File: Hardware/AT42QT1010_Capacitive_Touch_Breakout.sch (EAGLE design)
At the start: 31 parts, among them Q1 600mA/40V, U1 AT42QT1010 - UDFN

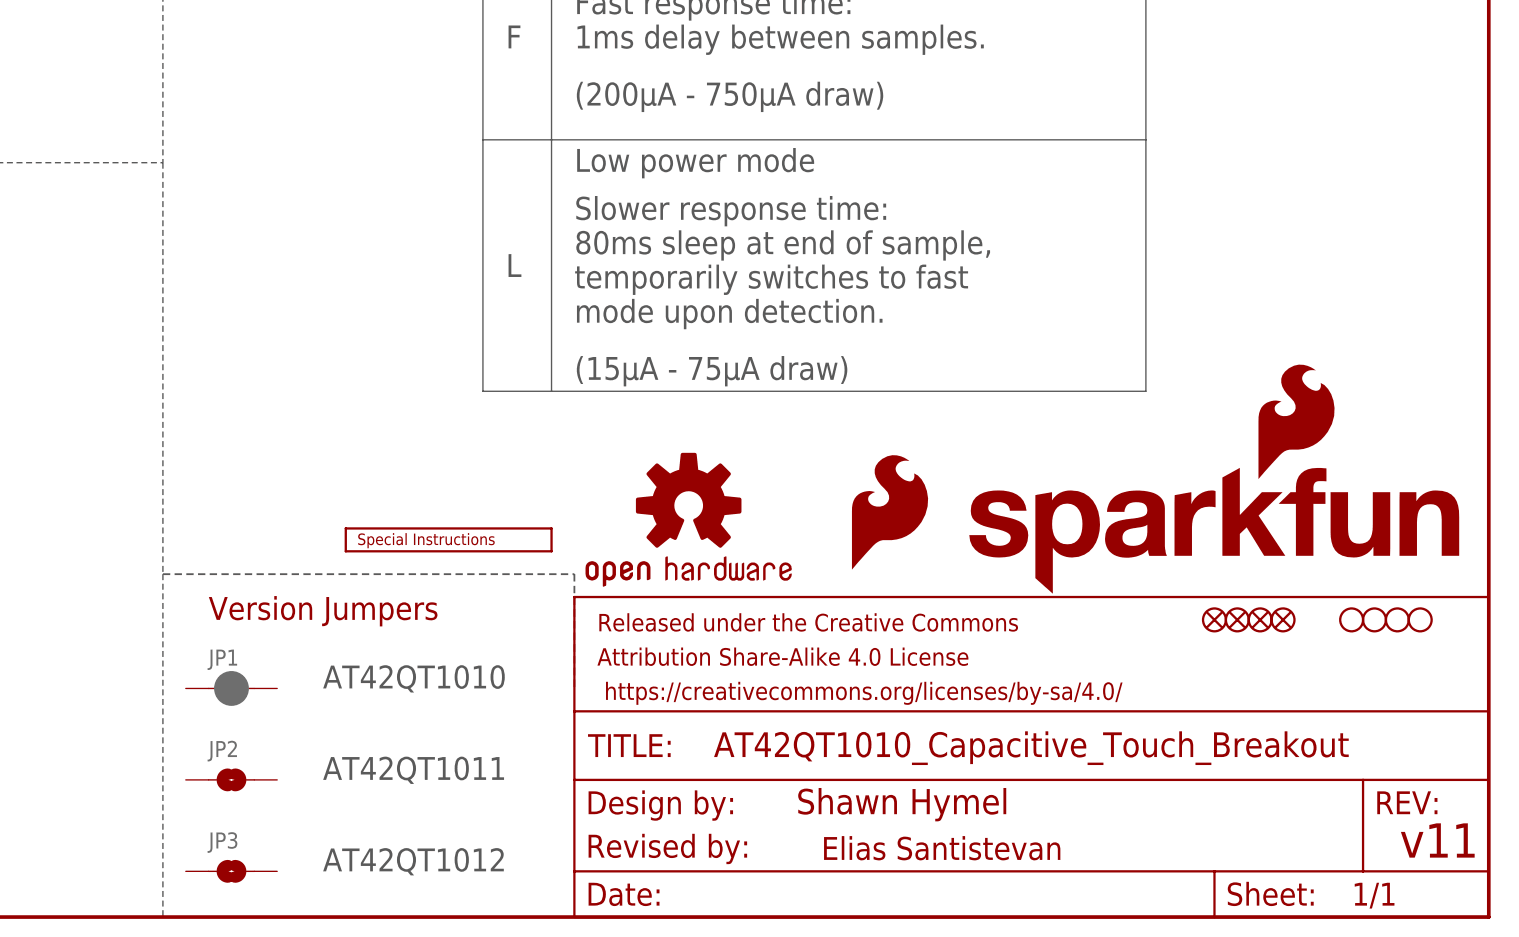
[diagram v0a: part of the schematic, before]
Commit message: Revert "Made space for and added version jumpers"
This reverts commit 0dfcf3fd33d472c1ea0c54a853371dbd5ffd3b83.
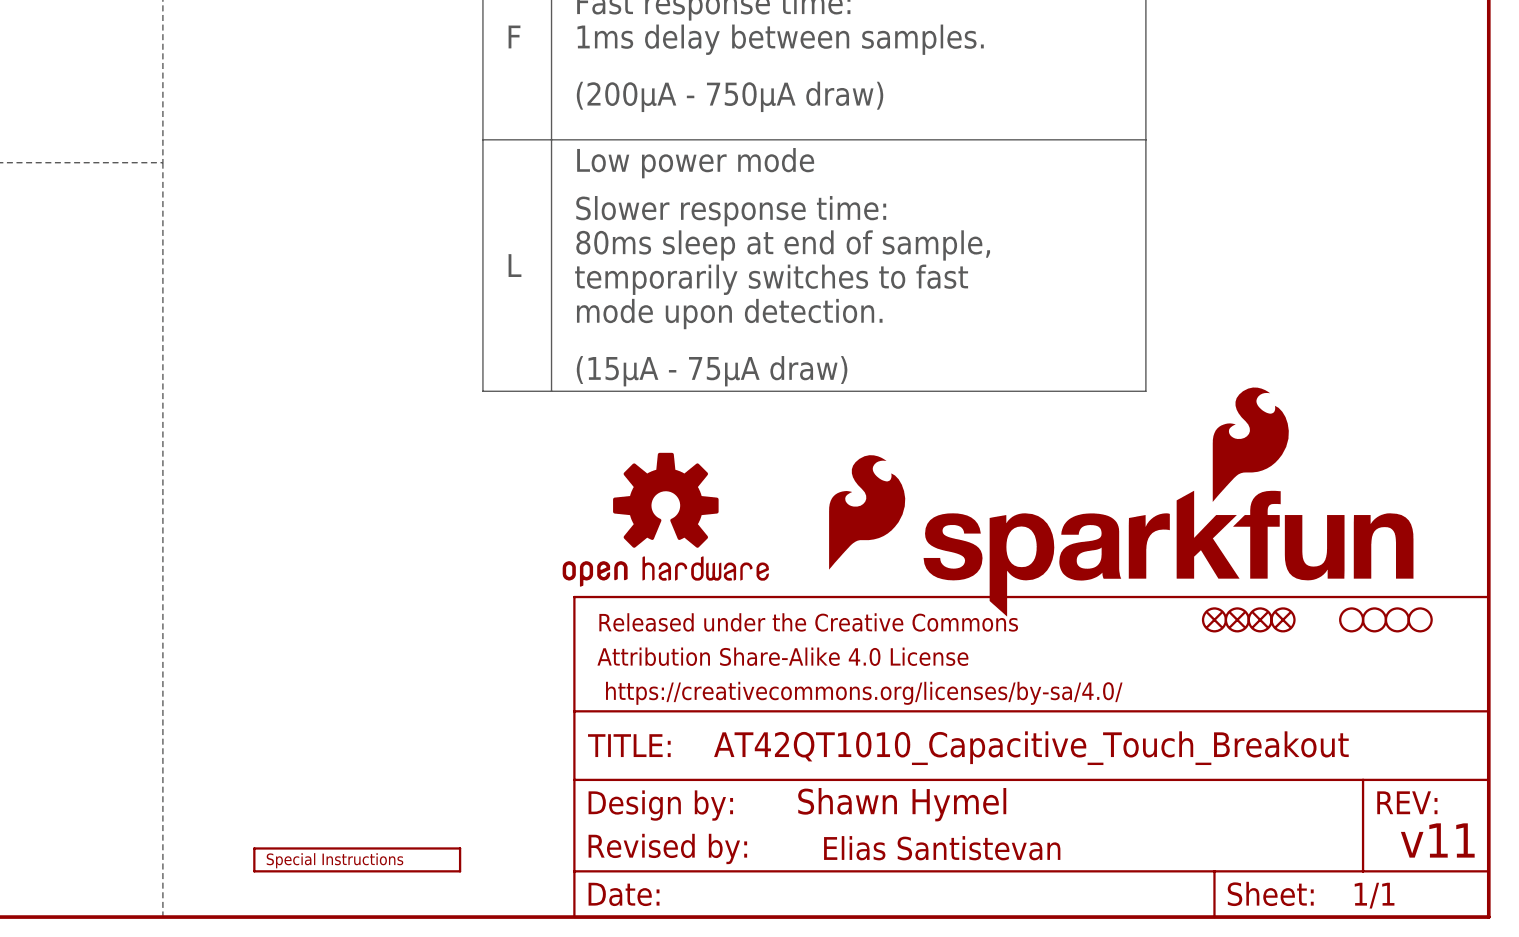
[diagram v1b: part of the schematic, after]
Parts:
- removed JP1: JUMPER-SMT_2_NC_PASTE_SILK, SparkFun-Jumpers:JUMPER-SMT_2_NC_PASTE_SILK
- removed JP2, JP3: JUMPER-SMT_2_NO_SILK, SparkFun-Jumpers:JUMPER-SMT_2_NO_SILK
- removed LOGO3: SFE_LOGO_NAME_FLAME.1_INCH, SparkFun-Aesthetics:SFE_LOGO_NAME_FLAME.1_INCH
- removed LOGO4: SFE_LOGO_FLAME.2_INCH, SparkFun-Aesthetics:SFE_LOGO_FLAME.2_INCH
- added LOGO1: SFE_LOGO_FLAME0.05_INCH, SparkFun-Aesthetics:SFE_LOGO_FLAME0.05_INCH
- added LOGO5: SFE_LOGO_NAME_WEB, SparkFun-Aesthetics:SFE_LOGO_NAME_WEB
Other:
- note removed: "AT42QT1010"
- note removed: "AT42QT1011"
- note removed: "AT42QT1012"
- note removed: "Version Jumpers"
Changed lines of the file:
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@@
 <part name="FID4" library="SparkFun-Aesthetics" deviceset="FIDUCIAL" device="1X2"/>
 <part name="JP7" library="SparkFun-Jumpers" deviceset="JUMPER-SMT_2_NO" device="_SILK"/>
+<part name="LOGO5" library="SparkFun-Aesthetics" deviceset="SFE_LOGO_NAME_WEB" device=""/>
 <part name="U$1" library="SparkFun-Aesthetics" deviceset="SPECIAL_INSTRUCTIONS" device="-ORDERING"/>
+<part name="LOGO1" library="SparkFun-Aesthetics" deviceset="SFE_LOGO_FLAME" device="0.05_INCH"/>
 <part name="J1" library="SparkFun-Connectors" deviceset="CONN_04" device=""/>
-<part name="LOGO3" library="SparkFun-Aesthetics" deviceset="SFE_LOGO_NAME_FLAME" device=".1_INCH"/>
-<part name="JP1" library="SparkFun-Jumpers" deviceset="JUMPER-SMT_2_NC_PASTE" device="_SILK"/>
-<part name="JP2" library="SparkFun-Jumpers" deviceset="JUMPER-SMT_2_NO" device="_SILK"/>
-<part name="JP3" library="SparkFun-Jumpers" deviceset="JUMPER-SMT_2_NO" device="_SILK"/>
-<part name="LOGO4" library="SparkFun-Aesthetics" deviceset="SFE_LOGO_FLAME" device=".2_INCH"/>
 </parts>
 <sheets>
@@
 <wire x1="101.6" y1="185.42" x2="101.6" y2="139.7" width="0.1524" layer="97" style="shortdash"/>
 <wire x1="101.6" y1="139.7" x2="101.6" y2="83.82" width="0.1524" layer="97" style="shortdash"/>
-<wire x1="101.6" y1="83.82" x2="101.6" y2="38.1" width="0.1524" layer="97" style="shortdash"/>
-<wire x1="101.6" y1="38.1" x2="101.6" y2="0" width="0.1524" layer="97" style="shortdash"/>
+<wire x1="101.6" y1="83.82" x2="101.6" y2="0" width="0.1524" layer="97" style="shortdash"/>
 <wire x1="0" y1="83.82" x2="101.6" y2="83.82" width="0.1524" layer="97" style="shortdash"/>
 <wire x1="0" y1="139.7" x2="101.6" y2="139.7" width="0.1524" layer="97" style="shortdash"/>
@@
 <wire x1="208.28" y1="127" x2="205.74" y2="127" width="0.2032" layer="97" style="shortdash"/>
 <wire x1="208.28" y1="112.776" x2="183.896" y2="112.776" width="0.2032" layer="97" style="shortdash"/>
-<wire x1="101.6" y1="38.1" x2="147.32" y2="38.1" width="0.2032" layer="97" style="shortdash"/>
-<wire x1="147.32" y1="38.1" x2="147.32" y2="25.4" width="0.2032" layer="97" style="shortdash"/>
-<text x="106.68" y="33.02" size="2.54" layer="94">Version Jumpers</text>
-<text x="119.38" y="25.4" size="2.54" layer="97">AT42QT1010</text>
-<text x="119.38" y="15.24" size="2.54" layer="97">AT42QT1011</text>
-<text x="119.38" y="5.08" size="2.54" layer="97">AT42QT1012</text>
 </plain>
 <instances>
@@
 <instance part="FRAME1" gate="G$1" x="0" y="0"/>
 <instance part="FRAME1" gate="V" x="147.32" y="0"/>
-<instance part="LOGO2" gate="G$1" x="160.02" y="45.72"/>
+<instance part="LOGO2" gate="G$1" x="157.48" y="45.72"/>
 <instance part="SUPPLY1" gate="G$1" x="165.1" y="157.48"/>
 <instance part="SUPPLY2" gate="G$1" x="60.96" y="124.46"/>
@@
 <attribute name="NAME" x="20.32" y="35.56" size="1.778" layer="95" font="vector"/>
 </instance>
-<instance part="U$1" gate="G$1" x="121.92" y="40.64"/>
+<instance part="LOGO5" gate="G$1" x="185.42" y="33.02"/>
+<instance part="U$1" gate="G$1" x="111.76" y="5.08"/>
+<instance part="LOGO1" gate="G$1" x="175.26" y="38.1"/>
 <instance part="J1" gate="G$1" x="45.72" y="109.22"/>
-<instance part="LOGO3" gate="G$1" x="190.5" y="35.56"/>
-<instance part="JP1" gate="G$1" x="109.22" y="25.4" smashed="yes">
-<attribute name="NAME" x="106.68" y="27.94" size="1.778" layer="95" font="vector"/>
-</instance>
-<instance part="JP2" gate="G$1" x="109.22" y="15.24" smashed="yes">
-<attribute name="NAME" x="106.68" y="17.78" size="1.778" layer="95" font="vector"/>
-</instance>
-<instance part="JP3" gate="G$1" x="109.22" y="5.08" smashed="yes">
-<attribute name="NAME" x="106.68" y="7.62" size="1.778" layer="95" font="vector"/>
-</instance>
-<instance part="LOGO4" gate="G$1" x="177.8" y="38.1"/>
 </instances>
 <busses>

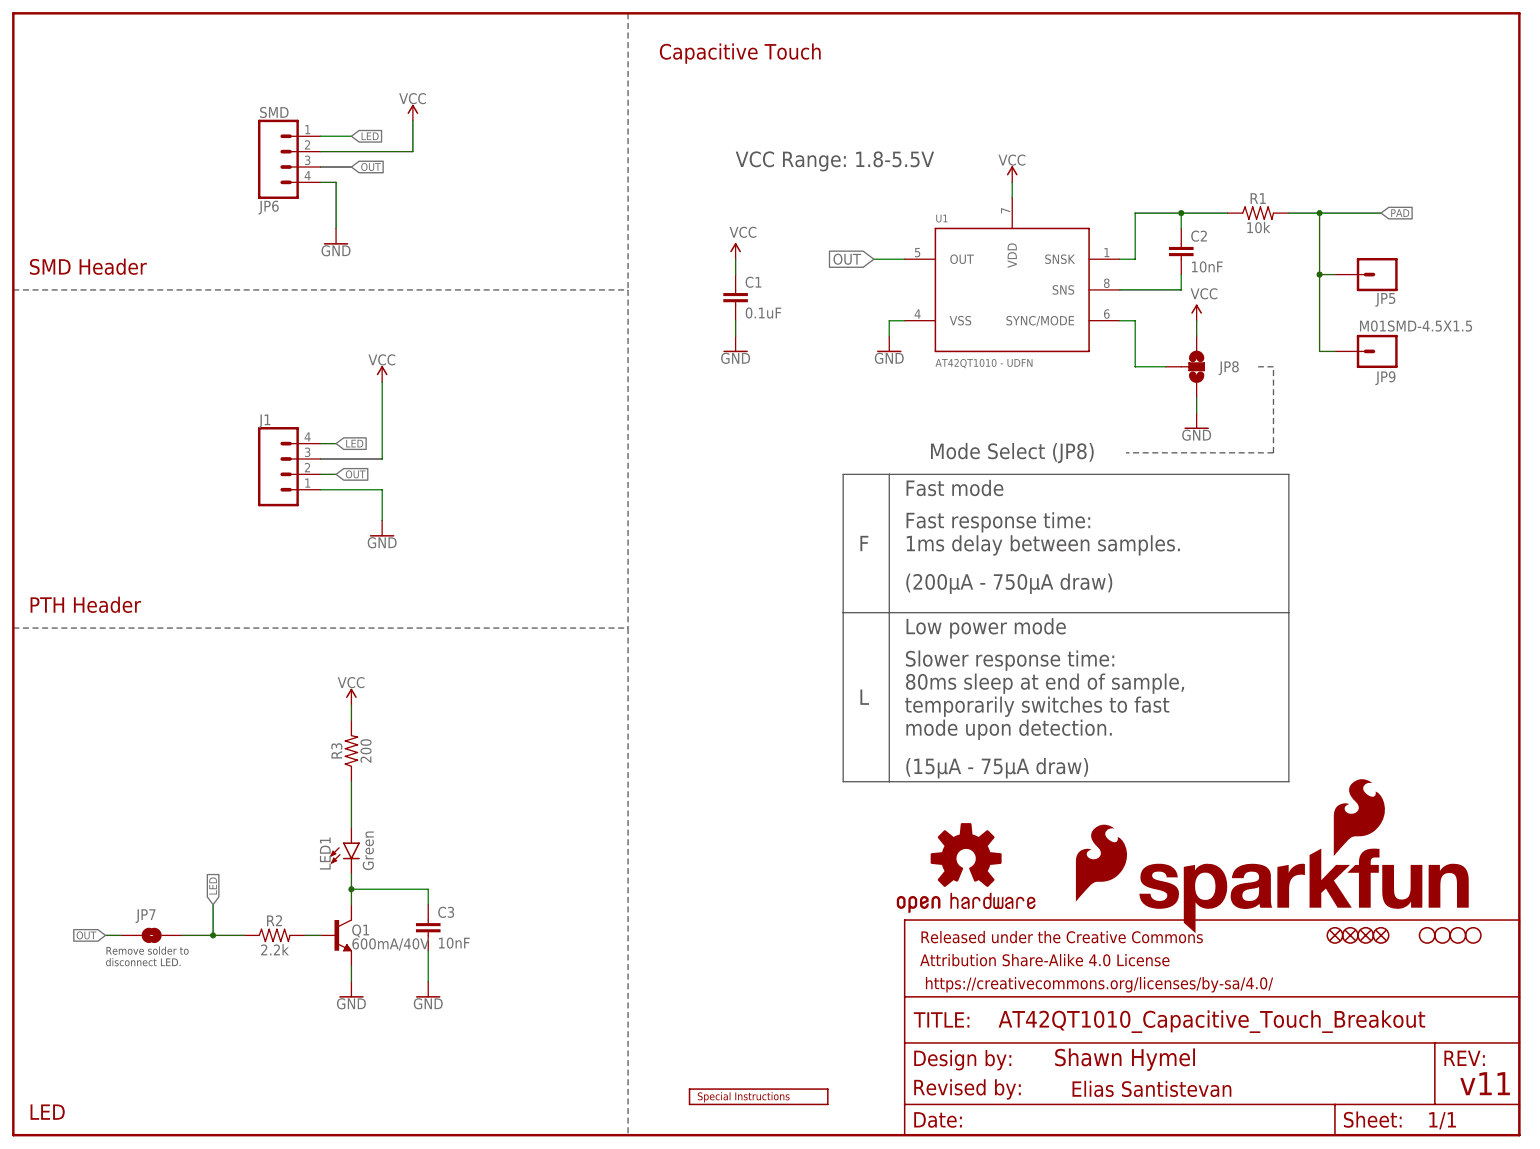
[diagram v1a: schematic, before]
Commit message: New branch due to the large changes to the existing direction of the product
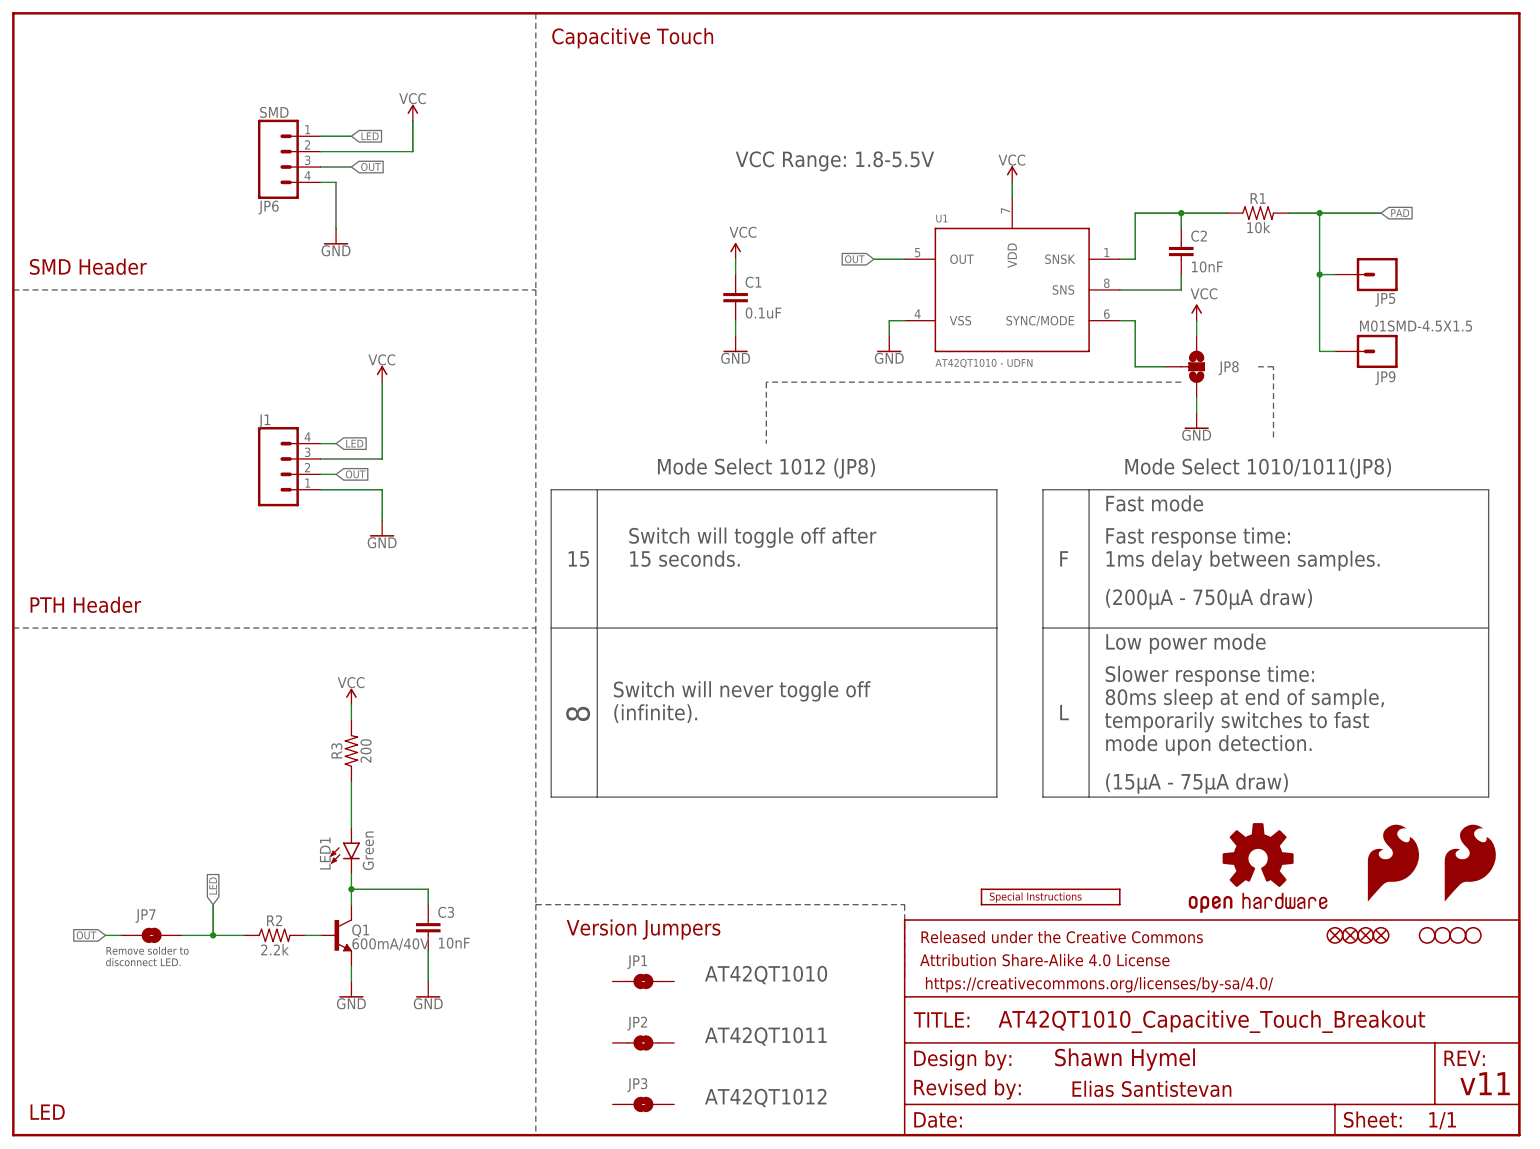
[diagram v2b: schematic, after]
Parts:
- removed LOGO5: SFE_LOGO_NAME_WEB, SparkFun-Aesthetics:SFE_LOGO_NAME_WEB
- added JP1, JP2, JP3: JUMPER-SMT_2_NO_SILK, SparkFun-Jumpers:JUMPER-SMT_2_NO_SILK
- added LOGO4: SFE_LOGO_FLAME.2_INCH, SparkFun-Aesthetics:SFE_LOGO_FLAME.2_INCH
- LOGO1: value SFE_LOGO_FLAME0.05_INCH -> SFE_LOGO_FLAME.2_INCH; device SparkFun-Aesthetics:SFE_LOGO_FLAME0.05_INCH -> SparkFun-Aesthetics:SFE_LOGO_FLAME.2_INCH
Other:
- note added: "15"
- note added: "8"
- note added: "AT42QT1010"
- note added: "AT42QT1011"
- note added: "AT42QT1012"
- note added: "Mode Select 1010/1011(JP8)"
- note added: "Mode Select 1012 (JP8)"
- note added: "Switch will never toggle off (infinite)."
- note added: "Switch will toggle off after 15 seconds."
- note added: "Version Jumpers"
- note removed: "Mode Select (JP8)"

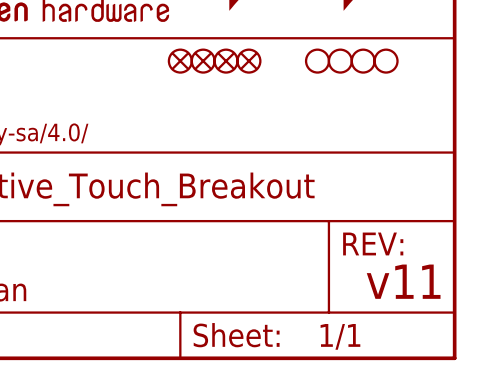
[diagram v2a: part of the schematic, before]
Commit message: Fixing text, changing version number
...in preparation for review.
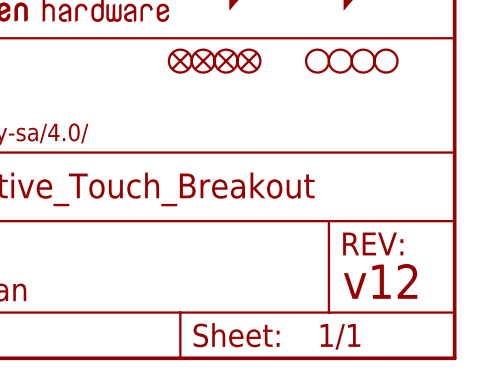
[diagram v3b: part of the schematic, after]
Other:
- note added: "v12"
- note removed: "v11"
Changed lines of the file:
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@@
 <sheet>
 <plain>
-<text x="171.958" y="11.43" size="2.794" layer="94">Shawn Hymel</text>
-<text x="239.014" y="6.604" size="3.81" layer="94">v11</text>
+<text x="171.958" y="11.43" size="2.794" layer="94" font="vector">Shawn Hymel</text>
+<text x="236.474" y="6.604" size="3.81" layer="94" font="vector">v12</text>
 <wire x1="86.36" y1="185.42" x2="86.36" y2="139.7" width="0.1524" layer="97" style="shortdash"/>
 <wire x1="86.36" y1="139.7" x2="86.36" y2="83.82" width="0.1524" layer="97" style="shortdash"/>
@@
 <wire x1="170.18" y1="83.82" x2="243.84" y2="83.82" width="0.1524" layer="97"/>
 <wire x1="177.8" y1="106.68" x2="177.8" y2="55.88" width="0.1524" layer="97"/>
-<text x="148.59" y="6.604" size="2.54" layer="94">Revised by:</text>
+<text x="148.59" y="6.604" size="2.54" layer="94" font="vector">Revised by:</text>
 <text x="174.752" y="6.35" size="2.54" layer="94" font="vector" ratio="10">Elias Santistevan</text>
 <text x="119.38" y="160.02" size="2.54" layer="97" font="vector">VCC Range: 1.8-5.5V</text>
-<text x="15.24" y="27.94" size="1.27" layer="97">Remove solder to
+<text x="15.24" y="27.94" size="1.27" layer="97" font="vector">Remove solder to
 disconnect LED.</text>
 <wire x1="208.28" y1="115.316" x2="208.28" y2="127" width="0.2032" layer="97" style="shortdash"/>
@@
 <wire x1="147.32" y1="38.1" x2="147.32" y2="25.4" width="0.2032" layer="97" style="shortdash"/>
 <text x="91.44" y="33.02" size="2.54" layer="94" font="vector">Version Jumpers</text>
-<text x="114.3" y="25.4" size="2.54" layer="97">AT42QT1010</text>
-<text x="114.3" y="15.24" size="2.54" layer="97">AT42QT1011</text>
-<text x="114.3" y="5.08" size="2.54" layer="97">AT42QT1012</text>
+<text x="114.3" y="25.4" size="2.54" layer="97" font="vector">AT42QT1010</text>
+<text x="114.3" y="15.24" size="2.54" layer="97" font="vector">AT42QT1011</text>
+<text x="114.3" y="5.08" size="2.54" layer="97" font="vector">AT42QT1012</text>
 <text x="91.44" y="93.98" size="2.54" layer="97" font="vector">15</text>
 <text x="91.44" y="71.12" size="3.81" layer="97" rot="R270">8</text>
